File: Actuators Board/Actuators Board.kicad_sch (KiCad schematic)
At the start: 82 parts, among them IC1 BD62120AEFJ-E2, J1 Conn_01x05_Male, J10 Conn_01x02_Male, J2 Solenoid(Sol), J4 Conn_01x03_Male, J5 Conn_01x06_Male, J9 Conn_01x02_Male, Q1 MMDT2222A, Q2 SI2366DS, U1 ESP32-PICO-D4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

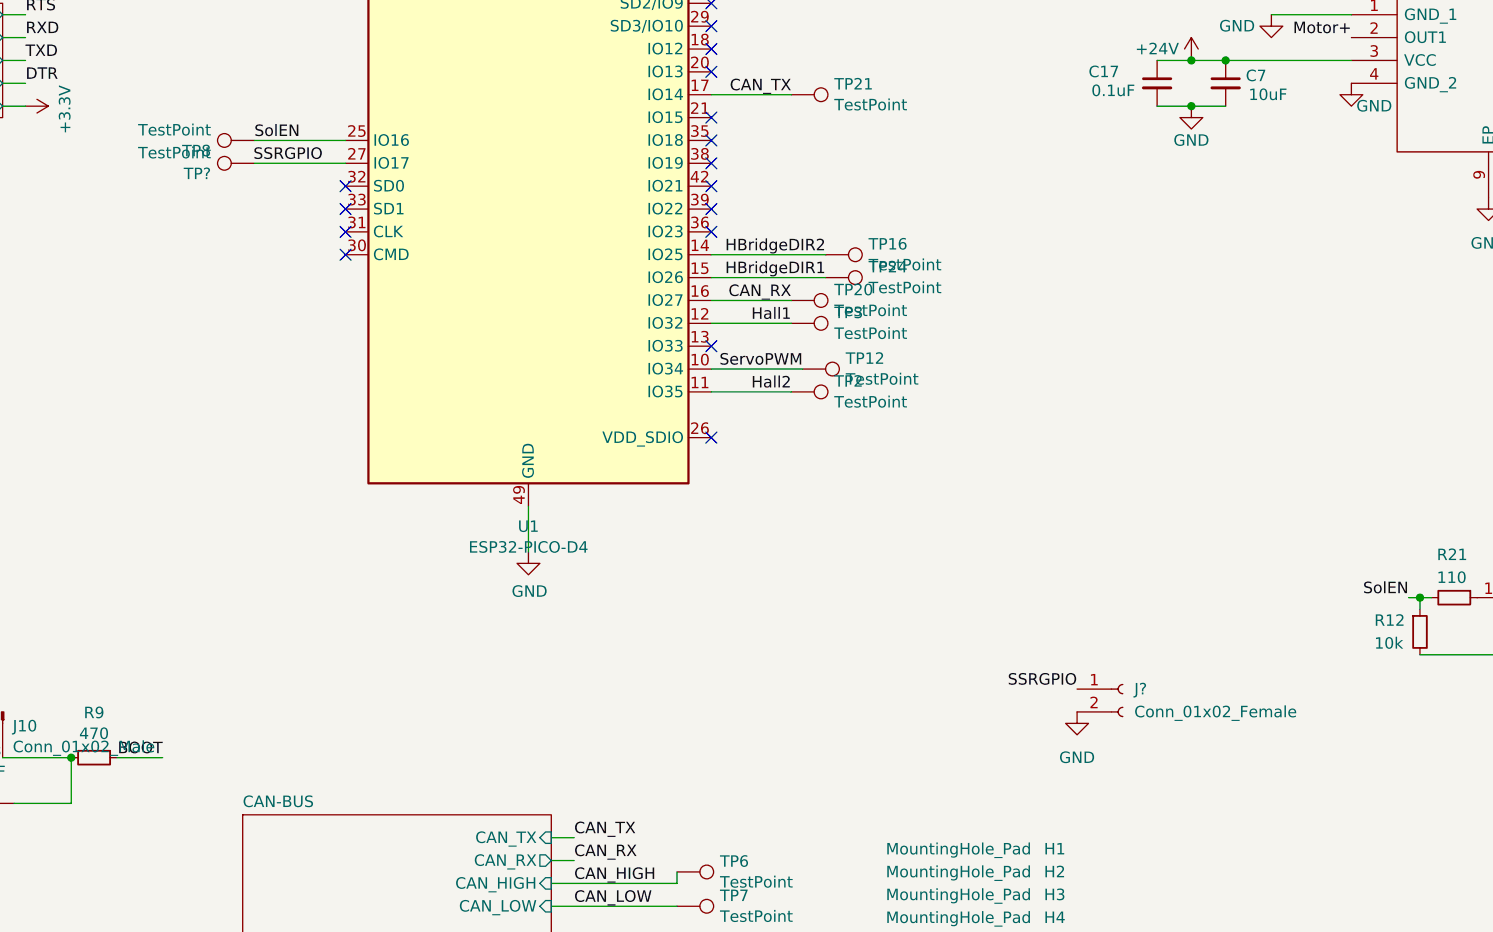
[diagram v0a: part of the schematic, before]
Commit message: Added solder jumpers and resistors for SSR pull-up and pull-down.
Also footprint assignment
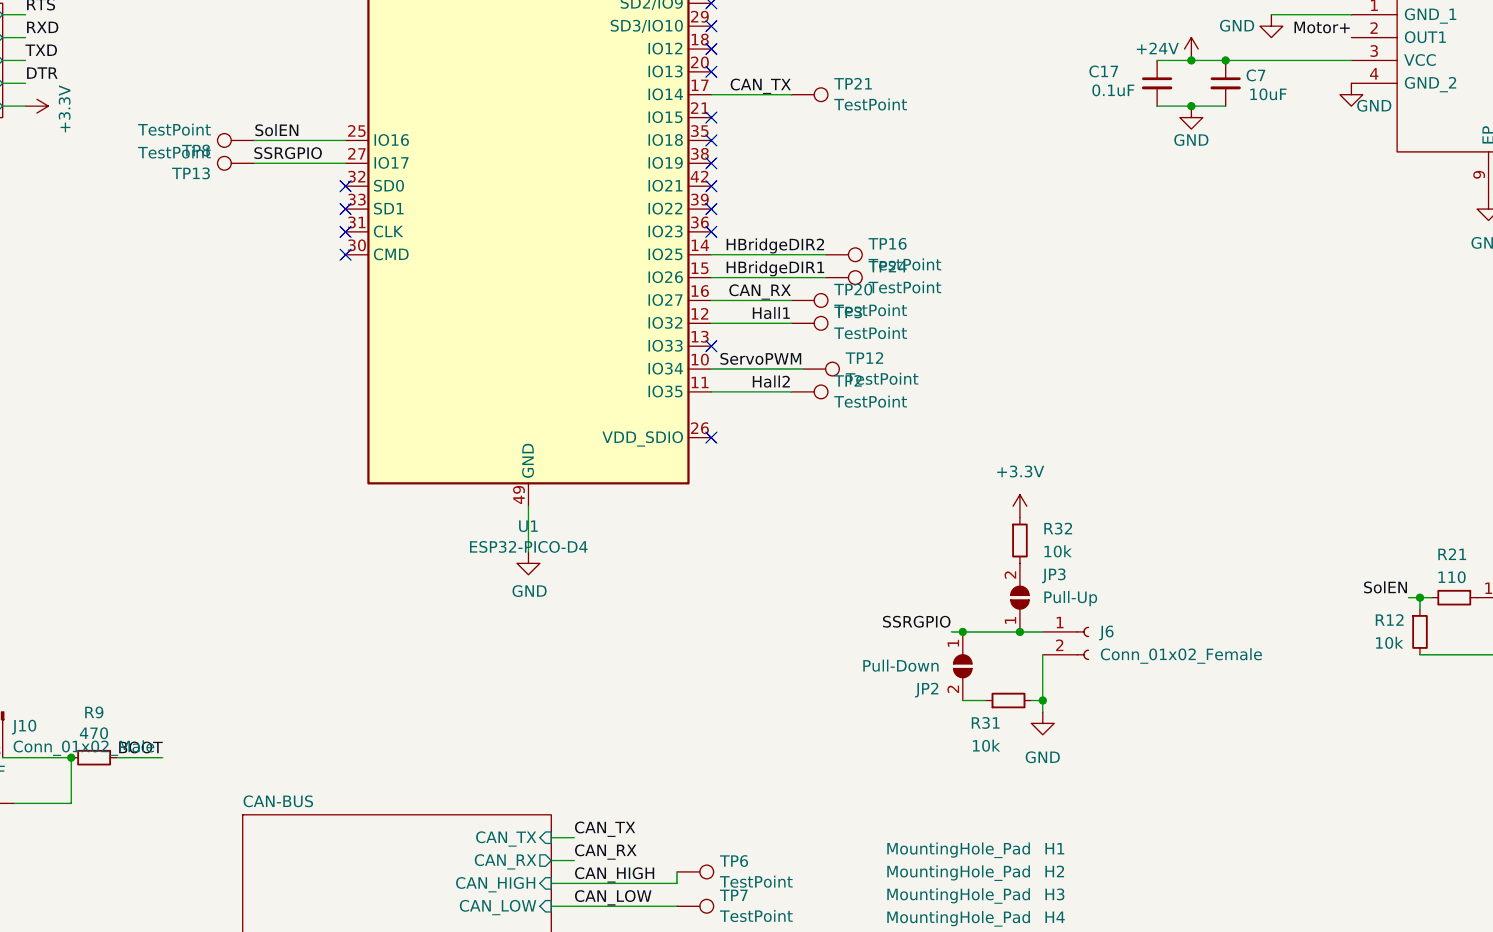
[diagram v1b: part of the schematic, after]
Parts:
- added JP2: Pull-Down, Jumper:SolderJumper-2_P1.3mm_Open_RoundedPad1.0x1.5mm, symbol Jumper:SolderJumper_2_Open
- added JP3: Pull-Up, Jumper:SolderJumper-2_P1.3mm_Open_RoundedPad1.0x1.5mm, symbol Jumper:SolderJumper_2_Open
- added R31, R32: 10k, Resistor_SMD:R_0603_1608Metric, symbol Device:R_Small
- J6: renamed from J?; footprint (none) -> Connector_PinHeader_2.54mm:PinHeader_1x02_P2.54mm_Vertical
- gave numbers to parts that had none: 1
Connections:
- net +3V3: now also R32.1
- net GND: now also R31.2
- net SSRGPIO: now also JP2.1 (A), JP3.1 (A)
- new net: JP2.2 (B), R31.1
- new net: JP3.2 (B), R32.2
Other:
- moved on the sheet: J6

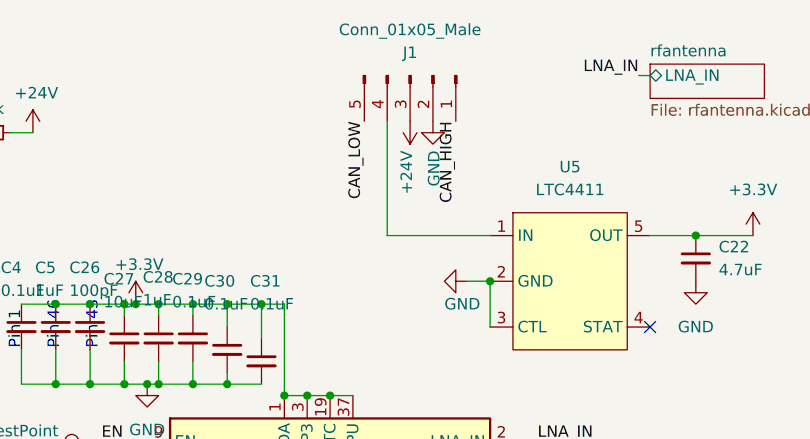
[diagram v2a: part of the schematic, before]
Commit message: Swapped RBUS connector, layout needs update.
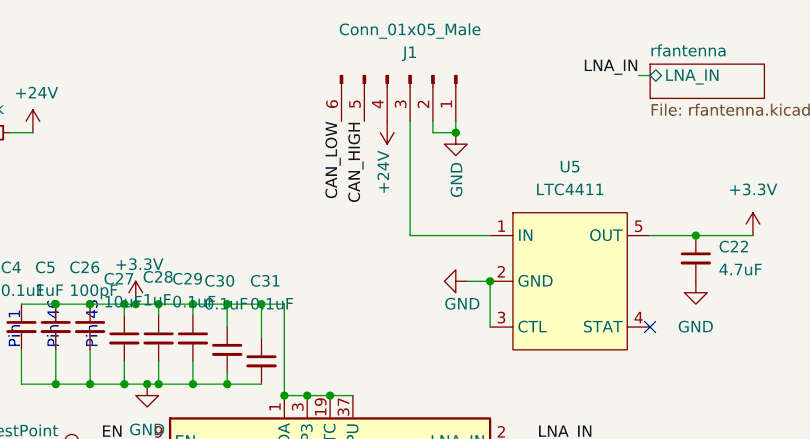
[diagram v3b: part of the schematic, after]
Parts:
- J1: footprint Connector_PinHeader_2.54mm:PinHeader_1x05_P2.54mm_Vertical -> Connector_Molex:Molex_Mini-Fit_Jr_5566-06A_2x03_P4.20mm_Vertical; symbol Connector:Conn_01x05_Male -> Connector:Conn_01x06_Male
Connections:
- net +24V: now also J1.4 (Pin_4); no longer J1.3 (Pin_3)
- net CAN_HIGH: now also J1.5 (Pin_5); no longer J1.1 (Pin_1)
- net CAN_LOW: now also J1.6 (Pin_6); no longer J1.5 (Pin_5)
- net GND: now also J1.1 (Pin_1)
- net at U5.1 (IN): now also J1.3 (Pin_3); no longer J1.4 (Pin_4)
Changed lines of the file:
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@@
   (junction (at 191.77 87.63) (diameter 0) (color 0 0 0 0)
   )
+  (junction (at 128.27 26.67) (diameter 0) (color 0 0 0 0)
+  )
   (junction (at 111.76 55.88) (diameter 0) (color 0 0 0 0)
   )
@@
   (no_connect (at 134.62 101.6))
   (no_connect (at 134.62 106.68))
-  (wire (pts (xy 120.65 38.1) (xy 132.08 38.1))
-    (stroke (width 0) (type default) (color 0 0 0 0))
-  )
   (wire (pts (xy 91.44 54.61) (xy 93.98 54.61))
     (stroke (width 0) (type default) (color 0 0 0 0))
@@
     (stroke (width 0) (type default) (color 0 0 0 0))
   )
+  (wire (pts (xy 128.27 25.4) (xy 128.27 26.67))
+    (stroke (width 0) (type default) (color 0 0 0 0))
+  )
   (wire (pts (xy 95.25 54.61) (xy 99.06 54.61))
     (stroke (width 0) (type default) (color 0 0 0 0))
@@
     (stroke (width 0) (type default) (color 0 0 0 0))
   )
+  (wire (pts (xy 125.73 26.67) (xy 128.27 26.67))
+    (stroke (width 0) (type default) (color 0 0 0 0))
+  )
   (wire (pts (xy 95.25 45.72) (xy 99.06 45.72))
     (stroke (width 0) (type default) (color 0 0 0 0))
@@
     (stroke (width 0) (type default) (color 0 0 0 0))
   )
+  (wire (pts (xy 123.19 25.4) (xy 123.19 38.1))
+    (stroke (width 0) (type default) (color 0 0 0 0))
+  )
   (wire (pts (xy 154.94 38.1) (xy 161.29 38.1))
     (stroke (width 0) (type default) (color 0 0 0 0))
@@
     (stroke (width 0) (type default) (color 0 0 0 0))
   )
+  (wire (pts (xy 125.73 25.4) (xy 125.73 26.67))
+    (stroke (width 0) (type default) (color 0 0 0 0))
+  )
   (wire (pts (xy 25.4 191.77) (xy 30.48 191.77))
     (stroke (width 0) (type default) (color 0 0 0 0))
@@
     (stroke (width 0) (type default) (color 0 0 0 0))
   )
+  (wire (pts (xy 123.19 38.1) (xy 132.08 38.1))
+    (stroke (width 0) (type default) (color 0 0 0 0))
+  )
   (wire (pts (xy 34.29 170.18) (xy 34.29 165.1))
     (stroke (width 0) (type default) (color 0 0 0 0))
@@
     (stroke (width 0) (type default) (color 0 0 0 0))
   )
-  (wire (pts (xy 120.65 25.4) (xy 120.65 38.1))
-    (stroke (width 0) (type default) (color 0 0 0 0))
-  )
   (wire (pts (xy 27.94 170.18) (xy 34.29 170.18))
     (stroke (width 0) (type default) (color 0 0 0 0))
@@
     (effects (font (size 1.27 1.27)) (justify right bottom))
   )
-  (label "CAN_LOW" (at 118.11 25.4 270)
+  (label "CAN_LOW" (at 115.57 25.4 270)
     (effects (font (size 1.27 1.27)) (justify right bottom))
   )
@@
     (effects (font (size 1.27 1.27)) (justify left bottom))
   )
-  (label "CAN_HIGH" (at 128.27 25.4 270)
+  (label "CAN_HIGH" (at 118.11 25.4 270)
     (effects (font (size 1.27 1.27)) (justify right bottom))
   )
@@
     (pin "1")
   )
-  (symbol (lib_id "power:+24V") (at 123.19 25.4 180) (unit 1)
+  (symbol (lib_id "power:+24V") (at 120.65 25.4 180) (unit 1)
     (in_bom yes) (on_board yes)
-    (property "Reference" "#PWR0139" (id 0) (at 123.19 21.59 0)
+    (property "Reference" "#PWR0139" (id 0) (at 120.65 21.59 0)
       (effects (font (size 1.27 1.27)) hide)
     )
-    (property "Value" "+24V" (id 1) (at 122.809 28.6512 90)
+    (property "Value" "+24V" (id 1) (at 120.269 28.6512 90)
       (effects (font (size 1.27 1.27)) (justify left))
     )
-    (property "Footprint" "" (id 2) (at 123.19 25.4 0)
+    (property "Footprint" "" (id 2) (at 120.65 25.4 0)
       (effects (font (size 1.27 1.27)) hide)
     )
-    (property "Datasheet" "" (id 3) (at 123.19 25.4 0)
+    (property "Datasheet" "" (id 3) (at 120.65 25.4 0)
       (effects (font (size 1.27 1.27)) hide)
     )
     (pin "1")
   )
-  (symbol (lib_id "power:GND") (at 125.73 25.4 0) (unit 1)
+  (symbol (lib_id "power:GND") (at 128.27 26.67 0) (unit 1)
     (in_bom yes) (on_board yes)
-    (property "Reference" "#PWR0138" (id 0) (at 125.73 31.75 0)
+    (property "Reference" "#PWR0138" (id 0) (at 128.27 33.02 0)
       (effects (font (size 1.27 1.27)) hide)
     )
-    (property "Value" "GND" (id 1) (at 125.857 28.6512 90)
+    (property "Value" "GND" (id 1) (at 128.397 29.9212 90)
       (effects (font (size 1.27 1.27)) (justify right))
     )
-    (property "Footprint" "" (id 2) (at 125.73 25.4 0)
+    (property "Footprint" "" (id 2) (at 128.27 26.67 0)
       (effects (font (size 1.27 1.27)) hide)
     )
-    (property "Datasheet" "" (id 3) (at 125.73 25.4 0)
+    (property "Datasheet" "" (id 3) (at 128.27 26.67 0)
       (effects (font (size 1.27 1.27)) hide)
     )
     (pin "1")
   )
-  (symbol (lib_id "Connector:Conn_01x05_Male") (at 123.19 20.32 270) (unit 1)
+  (symbol (lib_id "Connector:Conn_01x06_Male") (at 123.19 20.32 270) (unit 1)
     (in_bom yes) (on_board yes)
     (property "Reference" "J1" (id 0) (at 123.19 17.78 90))
     (property "Value" "Conn_01x05_Male" (id 1) (at 123.19 15.24 90))
-    (property "Footprint" "Connector_PinHeader_2.54mm:PinHeader_1x05_P2.54mm_Vertical" (id 2) (at 123.19 20.32 0)
+    (property "Footprint" "Connector_Molex:Molex_Mini-Fit_Jr_5566-06A_2x03_P4.20mm_Vertical" (id 2) (at 123.19 20.32 0)
       (effects (font (size 1.27 1.27)) hide)
     )
@@
     (pin "4")
     (pin "5")
+    (pin "6")
   )
   (symbol (lib_id "Connector:TestPoint") (at 143.51 73.66 270) (unit 1)
@@
     )
     (path "/00000000-0000-0000-0000-000061b03907"
-      (reference "J1") (unit 1) (value "Conn_01x05_Male") (footprint "Connector_PinHeader_2.54mm:PinHeader_1x05_P2.54mm_Vertical")
+      (reference "J1") (unit 1) (value "Conn_01x05_Male") (footprint "Connector_Molex:Molex_Mini-Fit_Jr_5566-06A_2x03_P4.20mm_Vertical")
     )
     (path "/00000000-0000-0000-0000-000061be7646"
@@
     )
     (path "/00000000-0000-0000-0000-000061942b9a/07d5c73c-8fc0-4762-b96b-d67536f8bc5f"
-      (reference "JP?") (unit 1) (value "SolderJumper_2_Open") (footprint "")
+      (reference "JP4") (unit 1) (value "SolderJumper_2_Open") (footprint "Jumper:SolderJumper-2_P1.3mm_Open_Pad1.0x1.5mm")
     )
     (path "/00000000-0000-0000-0000-000061a24258/00000000-0000-0000-0000-000061a4fe2f"

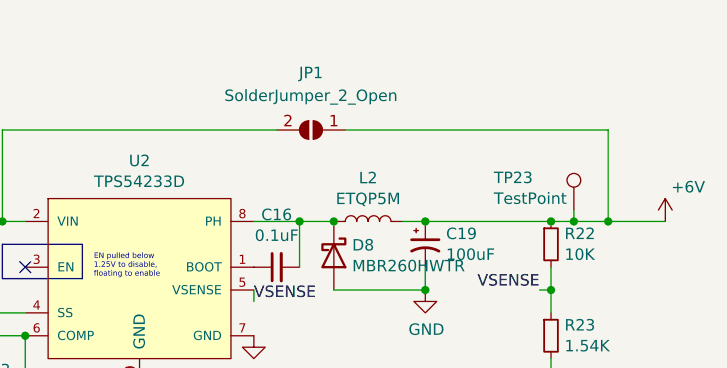
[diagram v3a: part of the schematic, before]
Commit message: Added CAN transceiver and new connector to board
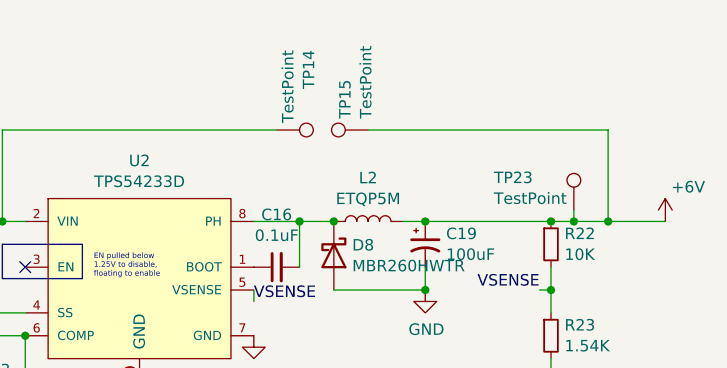
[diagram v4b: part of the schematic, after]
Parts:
- removed JP1: SolderJumper_2_Open, Jumper:SolderJumper-2_P1.3mm_Open_RoundedPad1.0x1.5mm, symbol Jumper:SolderJumper_2_Open
- added TP14, TP15: TestPoint, TestPoint:TestPoint_Pad_D2.0mm, symbol Connector:TestPoint
- TP1, TP10, TP11, TP12, TP13, TP16, TP2, TP23, TP24, TP3, TP4, TP5, TP8, TP9: footprint TestPoint:TestPoint_THTPad_1.0x1.0mm_Drill0.5mm -> TestPoint:TestPoint_Pad_D1.0mm
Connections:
- net +24V: now also TP14.1
- net +6V: now also TP15.1

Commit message: Changed connectors
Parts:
- J2: footprint Connector_PinHeader_2.54mm:PinHeader_1x02_P2.54mm_Vertical -> Connector_Molex:Molex_Nano-Fit_105309-xx02_1x02_P2.50mm_Vertical
- J4: footprint Connector_JST:JST_XH_B3B-XH-AM_1x03_P2.50mm_Vertical -> Connector_Molex:Molex_Nano-Fit_105309-xx03_1x03_P2.50mm_Vertical
- J5: footprint Connector_PinHeader_2.54mm:PinHeader_1x06_P2.54mm_Vertical -> Connector_Molex:Molex_Nano-Fit_105309-xx07_1x07_P2.50mm_Vertical
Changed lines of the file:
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@@
     (property "Reference" "J4" (id 0) (at 275.59 120.65 0))
     (property "Value" "Conn_01x03_Male" (id 1) (at 275.59 118.11 0))
-    (property "Footprint" "Connector_JST:JST_XH_B3B-XH-AM_1x03_P2.50mm_Vertical" (id 2) (at 278.13 127 0)
+    (property "Footprint" "Connector_Molex:Molex_Nano-Fit_105309-xx03_1x03_P2.50mm_Vertical" (id 2) (at 278.13 127 0)
       (effects (font (size 1.27 1.27)) hide)
     )
@@
       (effects (font (size 1.27 1.27)) (justify right))
     )
-    (property "Footprint" "Connector_PinHeader_2.54mm:PinHeader_1x02_P2.54mm_Vertical" (id 2) (at 259.08 142.24 0)
+    (property "Footprint" "Connector_Molex:Molex_Nano-Fit_105309-xx02_1x02_P2.50mm_Vertical" (id 2) (at 259.08 142.24 0)
       (effects (font (size 1.27 1.27)) hide)
     )
@@
     (property "Reference" "J5" (id 0) (at 274.32 81.28 0))
     (property "Value" "Conn_01x06_Male" (id 1) (at 274.32 83.82 0))
-    (property "Footprint" "Connector_PinHeader_2.54mm:PinHeader_1x06_P2.54mm_Vertical" (id 2) (at 283.21 95.25 0)
+    (property "Footprint" "Connector_Molex:Molex_Nano-Fit_105309-xx07_1x07_P2.50mm_Vertical" (id 2) (at 283.21 95.25 0)
       (effects (font (size 1.27 1.27)) hide)
     )
@@
     )
     (path "/00000000-0000-0000-0000-000061be7646"
-      (reference "J2") (unit 1) (value "Solenoid(Sol)") (footprint "Connector_PinHeader_2.54mm:PinHeader_1x02_P2.54mm_Vertical")
+      (reference "J2") (unit 1) (value "Solenoid(Sol)") (footprint "Connector_Molex:Molex_Nano-Fit_105309-xx02_1x02_P2.50mm_Vertical")
     )
     (path "/00000000-0000-0000-0000-000061925999/00000000-0000-0000-0000-000061988c49"
@@
     )
     (path "/00000000-0000-0000-0000-000061a7be4f"
-      (reference "J4") (unit 1) (value "Conn_01x03_Male") (footprint "Connector_JST:JST_XH_B3B-XH-AM_1x03_P2.50mm_Vertical")
+      (reference "J4") (unit 1) (value "Conn_01x03_Male") (footprint "Connector_Molex:Molex_Nano-Fit_105309-xx03_1x03_P2.50mm_Vertical")
     )
     (path "/00000000-0000-0000-0000-000061bfaac3"
-      (reference "J5") (unit 1) (value "Conn_01x06_Male") (footprint "Connector_PinHeader_2.54mm:PinHeader_1x06_P2.54mm_Vertical")
+      (reference "J5") (unit 1) (value "Conn_01x06_Male") (footprint "Connector_Molex:Molex_Nano-Fit_105309-xx07_1x07_P2.50mm_Vertical")
     )
     (path "/215f95ae-32c0-4801-b5d2-372b7548c088"

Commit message: Finished Board Layout
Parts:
- removed J6: Conn_01x02_Female, Connector_PinHeader_2.54mm:PinHeader_1x02_P2.54mm_Vertical, symbol Connector:Conn_01x02_Female
- removed JP2: Pull-Down, Jumper:SolderJumper-2_P1.3mm_Open_RoundedPad1.0x1.5mm, symbol Jumper:SolderJumper_2_Open
- removed JP3: Pull-Up, Jumper:SolderJumper-2_P1.3mm_Open_RoundedPad1.0x1.5mm, symbol Jumper:SolderJumper_2_Open
- removed TP20, TP21, TP23, TP6, TP7: TestPoint, TestPoint:TestPoint_Pad_D1.0mm, symbol Connector:TestPoint
- added R34, R35: 10k, Resistor_SMD:R_0603_1608Metric, symbol Device:R_Small
- added TP22, TP25: TestPoint, TestPoint:TestPoint_Pad_D1.5mm, symbol Connector:TestPoint
- J5: footprint Connector_Molex:Molex_Nano-Fit_105309-xx07_1x07_P2.50mm_Vertical -> Connector_Molex:Molex_Nano-Fit_105309-xx06_1x06_P2.50mm_Vertical
- TP8: footprint TestPoint:TestPoint_Pad_D1.0mm -> TestPoint:TestPoint_Pad_D1.5mm
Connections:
- net +3V3: now also R34.1, R35.1
- net GND: no longer IC1.9 (EP)
- net SSRGPIO: now also R31.1, R32.2, TP8.1, U1.6 (SENSOR_CAPP); no longer TP13.1, U1.27 (IO17)
- net SolEN: now also TP13.1, U1.28 (SD2/IO9); no longer TP8.1, U1.25 (IO16)
- new net ES1GPIO: R34.2, TP22.1, U1.25 (IO16)
- new net ES2GPIO: R35.2, TP25.1, U1.27 (IO17)
- no-connect marks 25 -> 23
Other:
- moved on the sheet: D7, R31, R32, R4
